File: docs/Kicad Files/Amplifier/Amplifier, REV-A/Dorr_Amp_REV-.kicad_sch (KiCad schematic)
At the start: 48 parts, among them J1 Speaker Terminals, J2 Input Terminals, J3 Power Input, Q1 2N3904, Q10 QD44H8G, Q2 QD45H8G, Q3 2N3904, Q4 2N3906, Q5 QD44H8G, Q6 2N3904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

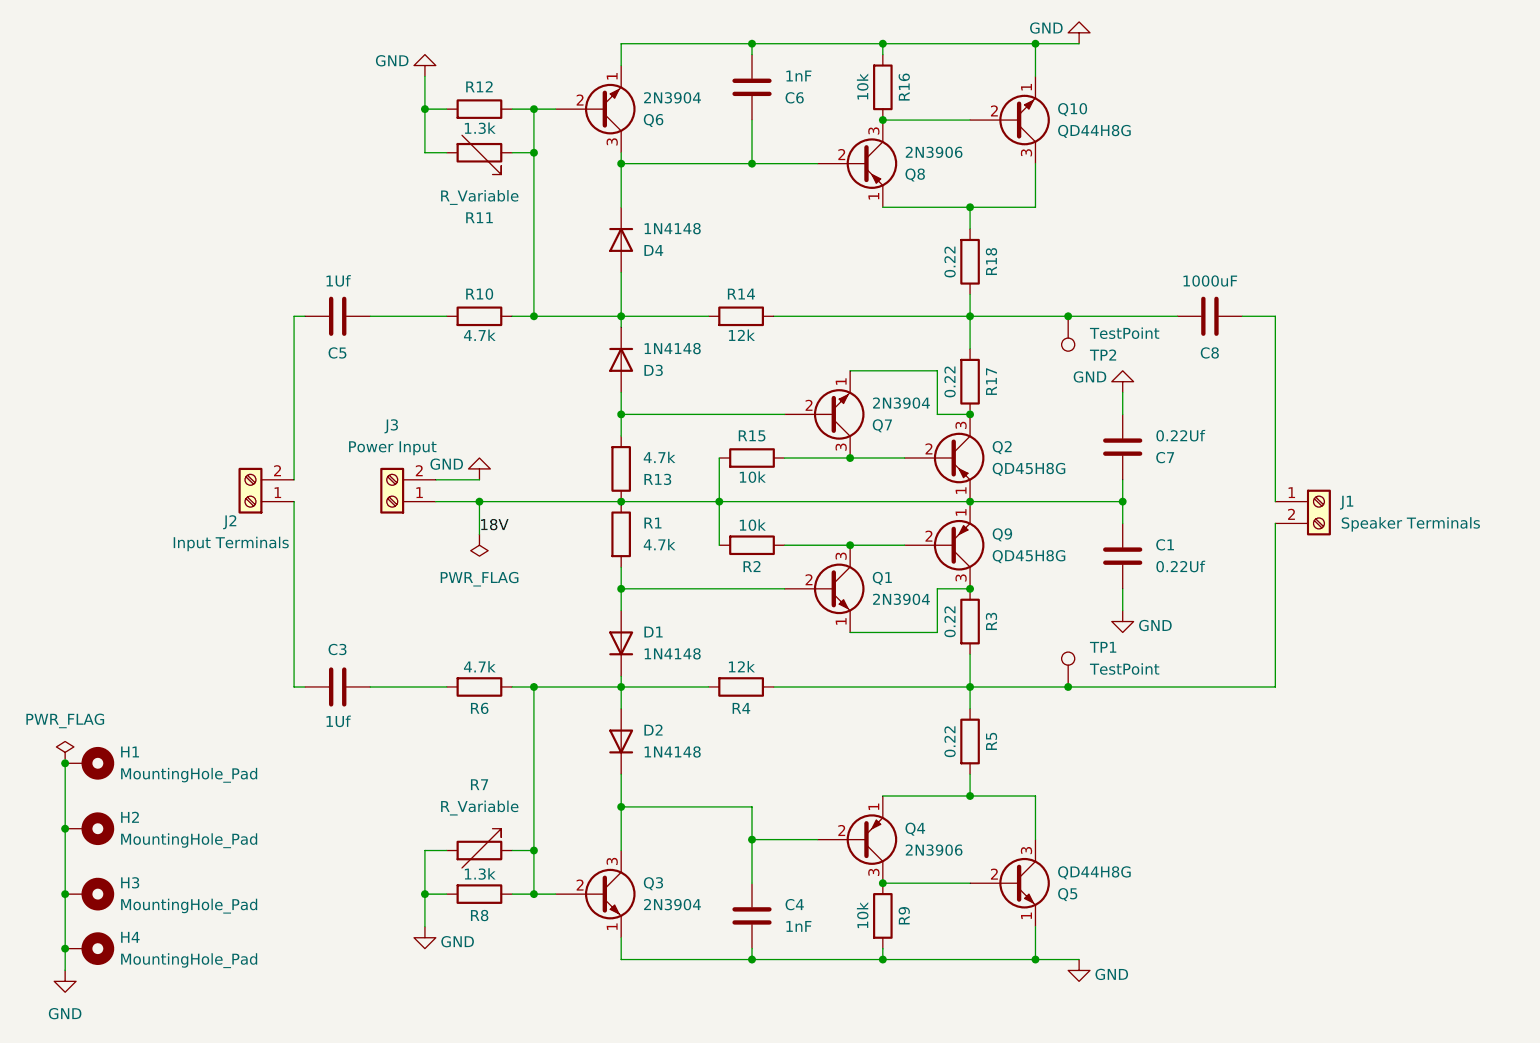
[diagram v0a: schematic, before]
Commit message: Amp Board Update
Updated the power transistor pins in the schematic to reflect datasheets. Minor changes to component placement.
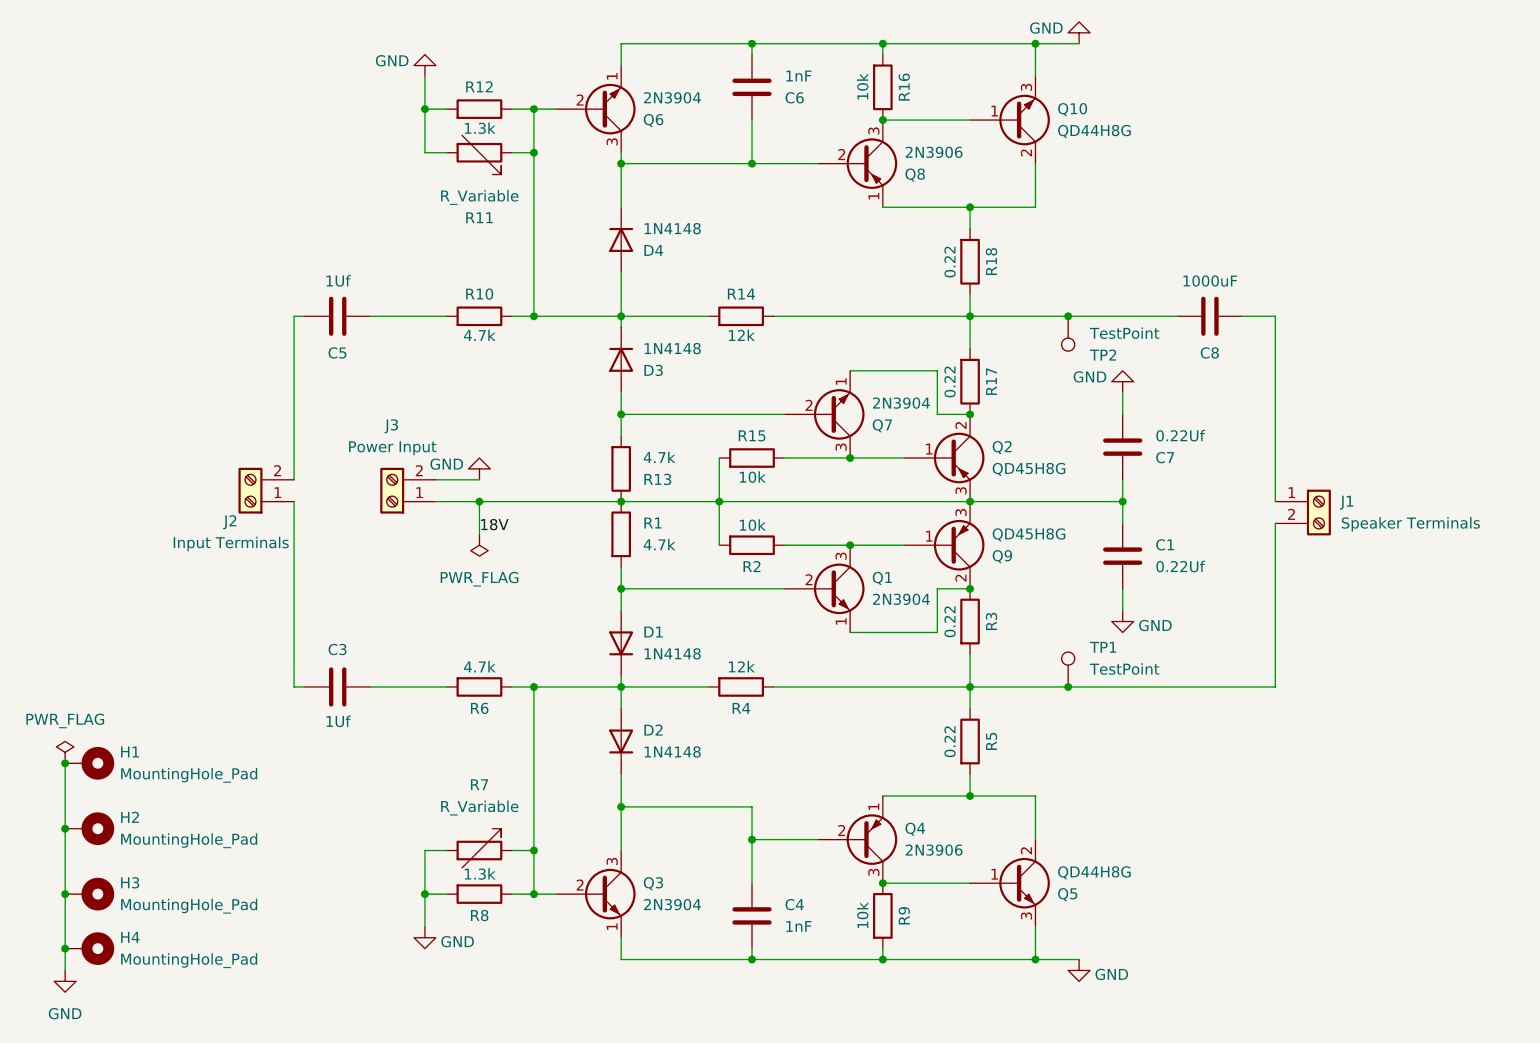
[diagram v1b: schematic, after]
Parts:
- Q10, Q2: footprint Package_TO_SOT_THT:TO-218-3_Vertical -> Package_TO_SOT_THT:TO-220-3_Vertical
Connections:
- net 18V: now also Q2.3 (E), Q9.3 (E); no longer Q2.1 (E), Q9.1 (E)
- net GND: now also Q10.3 (E), Q5.3 (E); no longer Q10.1 (E), Q5.1 (E)
- net at Q8.1 (E), R18.2: now also Q10.2 (C); no longer Q10.3 (C)
- net at Q1.3 (C), R2.1: now also Q9.1 (B); no longer Q9.2 (B)
- net at Q4.1 (E), R5.2: now also Q5.2 (C); no longer Q5.3 (C)
- net at Q8.3 (C), R16.1: now also Q10.1 (B); no longer Q10.2 (B)
- net at Q4.3 (C), R9.1: now also Q5.1 (B); no longer Q5.2 (B)
- net at Q7.1 (E), R17.1: now also Q2.2 (C); no longer Q2.3 (C)
- net at Q1.1 (E), R3.1: now also Q9.2 (C); no longer Q9.3 (C)
- net at Q7.3 (C), R15.1: now also Q2.1 (B); no longer Q2.2 (B)
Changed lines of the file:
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@@
 	)
 	(junction
-		(at 167.64 93.98)
-		(diameter 0)
-		(color 0 0 0 0)
-	)
-	(junction
 		(at 157.48 128.27)
 		(diameter 0)
@@
 	)
 	(junction
+		(at 167.64 93.98)
+		(diameter 0)
+		(color 0 0 0 0)
+	)
+	(junction
 		(at 175.26 30.48)
 		(diameter 0)
@@
 	)
 	(symbol
+		(lib_name "2N3904_1")
+		(lib_id "Transistor_BJT:2N3904")
+		(at 172.72 128.27 0)
+		(unit 1)
+		(exclude_from_sim no)
+		(in_bom yes)
+		(on_board yes)
+		(dnp no)
+		(property "Reference" "Q5"
+			(at 177.8 129.5401 0)
+			(effects
+				(font
+					(size 1.27 1.27)
+				)
+				(justify left)
+			)
+		)
+		(property "Value" "QD44H8G"
+			(at 177.8 127.0001 0)
+			(effects
+				(font
+					(size 1.27 1.27)
+				)
+				(justify left)
+			)
+		)
+		(property "Footprint" "Package_TO_SOT_THT:TO-220-3_Vertical"
+			(at 177.8 130.175 0)
+			(effects
+				(font
+					(size 1.27 1.27)
+					(italic yes)
+				)
+				(justify left)
+				(hide yes)
+			)
+		)
+		(property "Datasheet" "https://www.onsemi.com/pub/Collateral/2N3903-D.PDF"
+			(at 172.72 128.27 0)
+			(effects
+				(font
+					(size 1.27 1.27)
+				)
+				(justify left)
+				(hide yes)
+			)
+		)
+		(property "Description" "0.2A Ic, 40V Vce, Small Signal NPN Transistor, TO-92"
+			(at 172.72 128.27 0)
+			(effects
+				(font
+					(size 1.27 1.27)
+				)
+				(hide yes)
+			)
+		)
+		(pin "3"
+		)
+		(pin "1"
+		)
+		(pin "2"
+		)
+		(instances
+			(project "Dorr_Amp_REV-"
+				(path "/cc9ff92f-9b14-4efc-8fda-45ee1c134506"
+					(reference "Q5")
+					(unit 1)
+				)
+			)
+		)
+	)
+	(symbol
 		(lib_id "Device:C")
 		(at 185.42 77.47 0)
@@
 	)
 	(symbol
+		(lib_name "2N3906_1")
+		(lib_id "Transistor_BJT:2N3906")
+		(at 165.1 88.9 0)
+		(mirror x)
+		(unit 1)
+		(exclude_from_sim no)
+		(in_bom yes)
+		(on_board yes)
+		(dnp no)
+		(property "Reference" "Q9"
+			(at 170.18 90.1701 0)
+			(effects
+				(font
+					(size 1.27 1.27)
+				)
+				(justify left)
+			)
+		)
+		(property "Value" "QD45H8G"
+			(at 170.18 87.6301 0)
+			(effects
+				(font
+					(size 1.27 1.27)
+				)
+				(justify left)
+			)
+		)
+		(property "Footprint" "Package_TO_SOT_THT:TO-220-3_Vertical"
+			(at 170.18 86.995 0)
+			(effects
+				(font
+					(size 1.27 1.27)
+					(italic yes)
+				)
+				(justify left)
+				(hide yes)
+			)
+		)
+		(property "Datasheet" "https://www.onsemi.com/pub/Collateral/2N3906-D.PDF"
+			(at 165.1 88.9 0)
+			(effects
+				(font
+					(size 1.27 1.27)
+				)
+				(justify left)
+				(hide yes)
+			)
+		)
+		(property "Description" "-0.2A Ic, -40V Vce, Small Signal PNP Transistor, TO-92"
+			(at 165.1 88.9 0)
+			(effects
+				(font
+					(size 1.27 1.27)
+				)
+				(hide yes)
+			)
+		)
+		(pin "1"
+		)
+		(pin "3"
+		)
+		(pin "2"
+		)
+		(instances
+			(project "Dorr_Amp_REV-"
+				(path "/cc9ff92f-9b14-4efc-8fda-45ee1c134506"
+					(reference "Q9")
+					(unit 1)
+				)
+			)
+		)
+	)
+	(symbol
 		(lib_id "Connector:TestPoint")
 		(at 179.07 105.41 0)
@@
 	)
 	(symbol
+		(lib_name "2N3904_1")
 		(lib_id "Transistor_BJT:2N3904")
 		(at 172.72 39.37 0)
@@
 			)
 		)
-		(property "Footprint" "Package_TO_SOT_THT:TO-218-3_Vertical"
+		(property "Footprint" "Package_TO_SOT_THT:TO-220-3_Vertical"
 			(at 177.8 37.465 0)
 			(effects
@@
 	)
 	(symbol
-		(lib_id "Transistor_BJT:2N3904")
-		(at 172.72 128.27 0)
-		(unit 1)
-		(exclude_from_sim no)
-		(in_bom yes)
-		(on_board yes)
-		(dnp no)
-		(property "Reference" "Q5"
-			(at 177.8 129.5401 0)
-			(effects
-				(font
-					(size 1.27 1.27)
-				)
-				(justify left)
-			)
-		)
-		(property "Value" "QD44H8G"
-			(at 177.8 127.0001 0)
-			(effects
-				(font
-					(size 1.27 1.27)
-				)
-				(justify left)
-			)
-		)
-		(property "Footprint" "Package_TO_SOT_THT:TO-220-3_Vertical"
-			(at 177.8 130.175 0)
-			(effects
-				(font
-					(size 1.27 1.27)
-					(italic yes)
-				)
-				(justify left)
-				(hide yes)
-			)
-		)
-		(property "Datasheet" "https://www.onsemi.com/pub/Collateral/2N3903-D.PDF"
-			(at 172.72 128.27 0)
-			(effects
-				(font
-					(size 1.27 1.27)
-				)
-				(justify left)
-				(hide yes)
-			)
-		)
-		(property "Description" "0.2A Ic, 40V Vce, Small Signal NPN Transistor, TO-92"
-			(at 172.72 128.27 0)
-			(effects
-				(font
-					(size 1.27 1.27)
-				)
-				(hide yes)
-			)
-		)
-		(pin "3"
-		)
-		(pin "1"
-		)
-		(pin "2"
-		)
-		(instances
-			(project "Dorr_Amp_Draft3"
-				(path "/cc9ff92f-9b14-4efc-8fda-45ee1c134506"
-					(reference "Q5")
-					(unit 1)
-				)
-			)
-		)
-	)
-	(symbol
 		(lib_id "power:GND")
 		(at 185.42 96.52 0)
@@
 	)
 	(symbol
-		(lib_id "Transistor_BJT:2N3906")
-		(at 165.1 88.9 0)
-		(mirror x)
-		(unit 1)
-		(exclude_from_sim no)
-		(in_bom yes)
-		(on_board yes)
-		(dnp no)
-		(property "Reference" "Q9"
-			(at 170.18 87.6299 0)
-			(effects
-				(font
-					(size 1.27 1.27)
-				)
-				(justify left)
-			)
-		)
-		(property "Value" "QD45H8G"
-			(at 170.18 90.1699 0)
-			(effects
-				(font
-					(size 1.27 1.27)
-				)
-				(justify left)
-			)
-		)
-		(property "Footprint" "Package_TO_SOT_THT:TO-220-3_Vertical"
-			(at 170.18 86.995 0)
-			(effects
-				(font
-					(size 1.27 1.27)
-					(italic yes)
-				)
-				(justify left)
-				(hide yes)
-			)
-		)
-		(property "Datasheet" "https://www.onsemi.com/pub/Collateral/2N3906-D.PDF"
-			(at 165.1 88.9 0)
-			(effects
-				(font
-					(size 1.27 1.27)
-				)
-				(justify left)
-				(hide yes)
-			)
-		)
-		(property "Description" "-0.2A Ic, -40V Vce, Small Signal PNP Transistor, TO-92"
-			(at 165.1 88.9 0)
-			(effects
-				(font
-					(size 1.27 1.27)
-				)
-				(hide yes)
-			)
-		)
-		(pin "1"
-		)
-		(pin "3"
-		)
-		(pin "2"
-		)
-		(instances
-			(project "Dorr_Amp_Draft3"
-				(path "/cc9ff92f-9b14-4efc-8fda-45ee1c134506"
-					(reference "Q9")
-					(unit 1)
-				)
-			)
-		)
-	)
-	(symbol
 		(lib_id "Connector:Screw_Terminal_01x02")
 		(at 208.28 83.82 0)
@@
 	)
 	(symbol
+		(lib_name "2N3906_1")
 		(lib_id "Transistor_BJT:2N3906")
 		(at 165.1 78.74 0)
@@
 			)
 		)
-		(property "Footprint" "Package_TO_SOT_THT:TO-218-3_Vertical"
+		(property "Footprint" "Package_TO_SOT_THT:TO-220-3_Vertical"
 			(at 170.18 80.645 0)
 			(effects
